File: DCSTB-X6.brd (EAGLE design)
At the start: 29 x 70 mm, 5 parts

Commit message: Changed board texts. Generated CAM files. Generated PDF schematics.
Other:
- board text added: "DCSTB-X6-0010 (c) Andriy Golovnya http://redscorp.net"
- board text removed: "DC-STB-X6-0010 (c) Andriy Golovnya http://redscorp.net"
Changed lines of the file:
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@@
 <drawing>
 <settings>
-<setting alwaysvectorfont="yes"/>
+<setting alwaysvectorfont="no"/>
 <setting verticaltext="up"/>
 </settings>
@@
 <circle x="15" y="4" radius="4.5" width="0.127" layer="51"/>
 <circle x="15" y="66" radius="4.5" width="0.127" layer="51"/>
-<text x="28" y="46" size="1.778" layer="22" font="vector" rot="MR270">DC-STB-X6-0010
+<text x="28" y="46" size="1.778" layer="22" font="vector" rot="MR270">DCSTB-X6-0010
 (c) Andriy Golovnya
 http://redscorp.net</text>

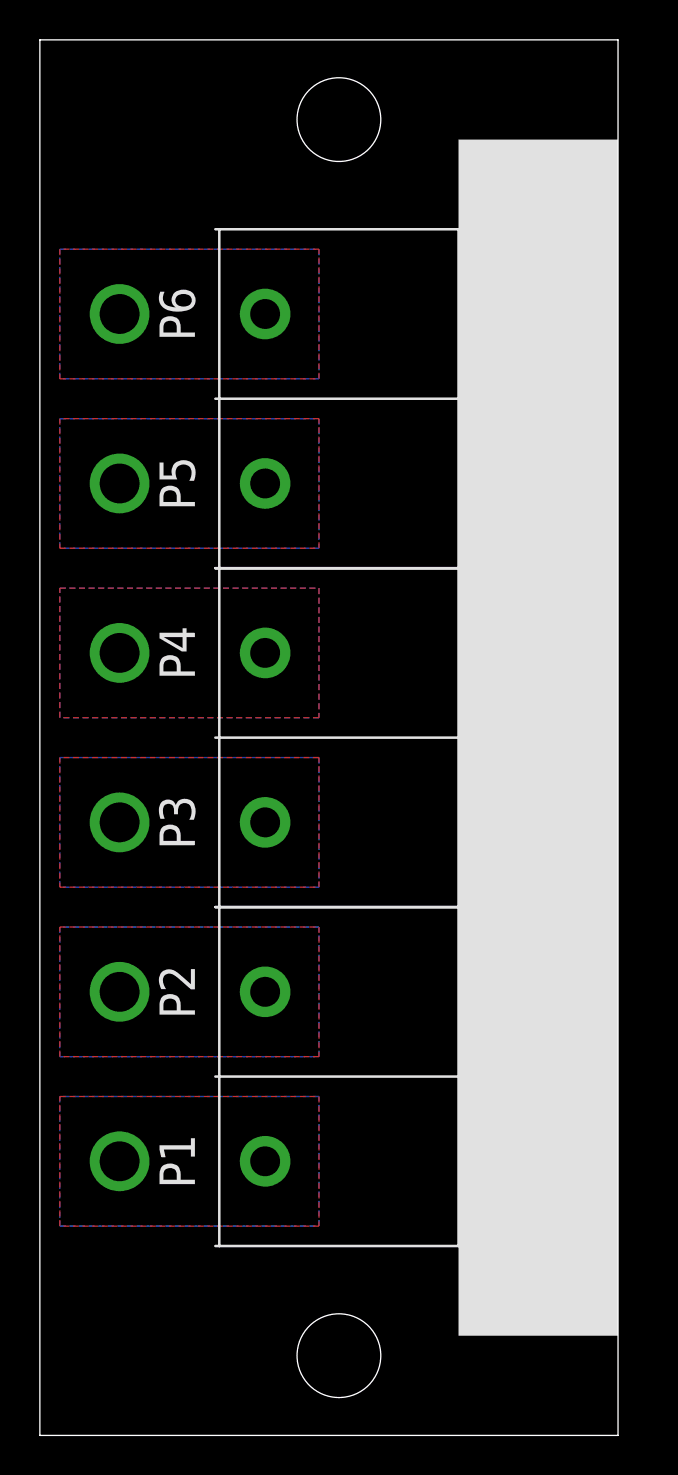
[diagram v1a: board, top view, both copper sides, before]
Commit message: Made boards a little bigger. Generated PNG preview. Generated CAM files.
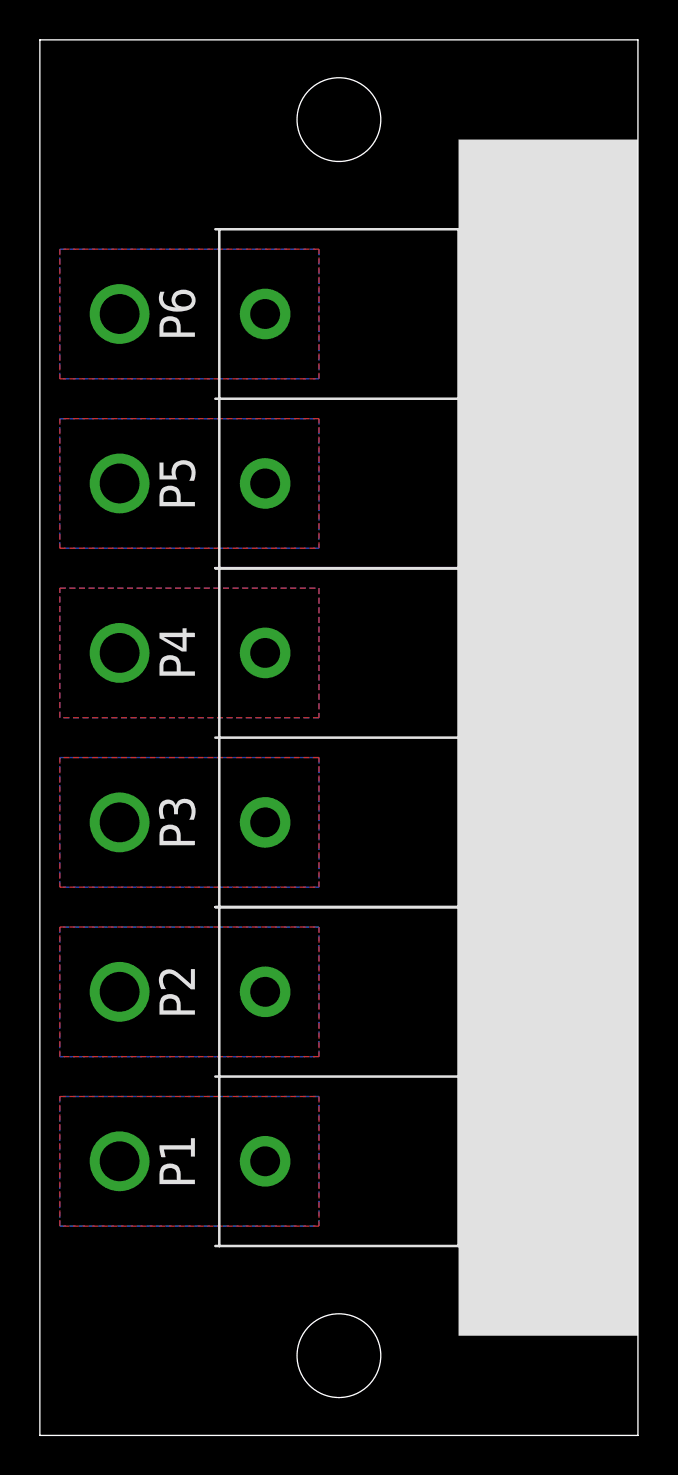
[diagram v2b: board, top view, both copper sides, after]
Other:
- board size 29 x 70 mm -> 30 x 70 mm
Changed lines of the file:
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@@
 <drawing>
 <settings>
-<setting alwaysvectorfont="no"/>
+<setting alwaysvectorfont="yes"/>
 <setting verticaltext="up"/>
 </settings>
@@
 <board>
 <plain>
-<wire x1="0" y1="0" x2="29" y2="0" width="0" layer="20"/>
-<wire x1="29" y1="0" x2="29" y2="70" width="0" layer="20"/>
-<wire x1="29" y1="70" x2="0" y2="70" width="0" layer="20"/>
+<wire x1="0" y1="0" x2="30" y2="0" width="0" layer="20"/>
+<wire x1="30" y1="0" x2="30" y2="70" width="0" layer="20"/>
+<wire x1="30" y1="70" x2="0" y2="70" width="0" layer="20"/>
 <wire x1="0" y1="70" x2="0" y2="0" width="0" layer="20"/>
 <hole x="15" y="4" drill="4.2"/>
@@
 <circle x="15" y="4" radius="4.5" width="0.127" layer="51"/>
 <circle x="15" y="66" radius="4.5" width="0.127" layer="51"/>
-<text x="28" y="46" size="1.778" layer="22" font="vector" rot="MR270">DCSTB-X6-0010
+<text x="29" y="46" size="1.778" layer="22" font="vector" rot="MR270">DCSTB-X6-0010
 (c) Andriy Golovnya
 http://redscorp.net</text>
-<rectangle x1="21" y1="5" x2="29" y2="65" layer="21"/>
+<rectangle x1="21" y1="5" x2="30" y2="65" layer="21"/>
 <text x="6" y="13.75" size="1.778" layer="21" font="vector" rot="R90" align="top-center">P1</text>
 <text x="6" y="22.25" size="1.778" layer="21" font="vector" rot="R90" align="top-center">P2</text>
